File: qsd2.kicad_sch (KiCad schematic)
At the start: 73 parts, among them J1 5-1814832-1, J2 5-1814832-1, J3 Conn_02x08_Odd_Even, J4 SJ-3524-SMT, U1 SN74LVC1G14DBV, U10 GALI-39, U2 SN74LVC1G14DBV, U3 SN74CBT3253, U4 SN74AC74PW, U5 AD8226ARZ-R7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

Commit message: Minor updates to schematic.
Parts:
- C20, C21: value 1nF -> Not used
- R3: value 250 -> 220
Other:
- note added: "5V or 3.3V Option for quadrature and demodulator devices. Place R29 or R30 as required for the chosen device voltage tolerance."
- note removed: "5V or 3.3V Option for demodulator"
- moved on the sheet: R29, R30
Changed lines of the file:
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@@
   (junction (at 91.44 34.29) (diameter 0) (color 0 0 0 0)
   )
-  (junction (at 113.665 146.05) (diameter 0) (color 0 0 0 0)
+  (junction (at 103.505 141.605) (diameter 0) (color 0 0 0 0)
   )
   (junction (at 38.735 170.815) (diameter 0) (color 0 0 0 0)
@@
     (stroke (width 0) (type default))
   )
-  (wire (pts (xy 108.585 141.605) (xy 113.665 141.605))
+  (wire (pts (xy 98.425 137.16) (xy 103.505 137.16))
     (stroke (width 0) (type default))
   )
@@
     (stroke (width 0) (type default))
   )
-  (wire (pts (xy 103.505 151.13) (xy 94.615 151.13))
+  (wire (pts (xy 93.345 146.685) (xy 84.455 146.685))
     (stroke (width 0) (type default))
   )
@@
     (stroke (width 0) (type default))
   )
-  (wire (pts (xy 113.665 146.05) (xy 121.285 146.05))
+  (wire (pts (xy 103.505 141.605) (xy 111.125 141.605))
     (stroke (width 0) (type default))
   )
@@
     (stroke (width 0) (type default))
   )
-  (wire (pts (xy 113.665 146.05) (xy 113.665 151.13))
+  (wire (pts (xy 103.505 141.605) (xy 103.505 146.685))
     (stroke (width 0) (type default))
   )
@@
     (stroke (width 0) (type default))
   )
-  (wire (pts (xy 94.615 141.605) (xy 103.505 141.605))
+  (wire (pts (xy 84.455 137.16) (xy 93.345 137.16))
     (stroke (width 0) (type default))
   )
@@
     (stroke (width 0) (type default))
   )
-  (wire (pts (xy 113.665 141.605) (xy 113.665 146.05))
+  (wire (pts (xy 103.505 137.16) (xy 103.505 141.605))
     (stroke (width 0) (type default))
   )
@@
     (stroke (width 0) (type default))
   )
-  (wire (pts (xy 108.585 151.13) (xy 113.665 151.13))
+  (wire (pts (xy 98.425 146.685) (xy 103.505 146.685))
     (stroke (width 0) (type default))
   )
@@
     (effects (font (size 2 2) bold) (justify left bottom))
   )
-  (text "5V or 3.3V Option\nfor demodulator" (at 116.84 153.035 0)
+  (text "5V or 3.3V Option\nfor quadrature and demodulator\ndevices.  Place R29 or R30 as\nrequired for the chosen device\nvoltage tolerance."
+    (at 105.41 153.67 0)
     (effects (font (size 1.27 1.27)) (justify left bottom))
   )
@@
     (effects (font (size 1.27 1.27)) (justify left bottom))
   )
-  (label "3_3V_FILT" (at 94.615 151.13 0) (fields_autoplaced)
+  (label "3_3V_FILT" (at 84.455 146.685 0) (fields_autoplaced)
     (effects (font (size 1.27 1.27)) (justify left bottom))
   )
-  (label "QSD_V" (at 121.285 146.05 0) (fields_autoplaced)
+  (label "QSD_V" (at 111.125 141.605 0) (fields_autoplaced)
     (effects (font (size 1.27 1.27)) (justify left bottom))
   )
-  (label "5V_FILT" (at 94.615 141.605 0) (fields_autoplaced)
+  (label "5V_FILT" (at 84.455 137.16 0) (fields_autoplaced)
     (effects (font (size 1.27 1.27)) (justify left bottom))
   )
@@
     )
   )
-  (symbol (lib_id "Device:R_Small_US") (at 106.045 151.13 90) (unit 1)
+  (symbol (lib_id "Device:R_Small_US") (at 95.885 146.685 90) (unit 1)
     (in_bom yes) (on_board yes) (dnp no) (fields_autoplaced)
-    (property "Reference" "R30" (at 106.045 145.415 90)
+    (property "Reference" "R30" (at 95.885 140.97 90)
       (effects (font (size 1.27 1.27)))
     )
-    (property "Value" "0" (at 106.045 147.955 90)
+    (property "Value" "0" (at 95.885 143.51 90)
       (effects (font (size 1.27 1.27)))
     )
-    (property "Footprint" "Resistor_SMD:R_1206_3216Metric" (at 106.045 151.13 0)
+    (property "Footprint" "Resistor_SMD:R_1206_3216Metric" (at 95.885 146.685 0)
       (effects (font (size 1.27 1.27)) hide)
     )
-    (property "Datasheet" "~" (at 106.045 151.13 0)
+    (property "Datasheet" "~" (at 95.885 146.685 0)
       (effects (font (size 1.27 1.27)) hide)
     )
@@
   (symbol (lib_id "Device:R_Small_US") (at 55.245 93.98 0) (unit 1)
     (in_bom yes) (on_board yes) (dnp no) (fields_autoplaced)
-    (property "Reference" "R3" (at 57.785 92.71 0)
+    (property "Reference" "R3" (at 57.15 92.71 0)
       (effects (font (size 1.27 1.27)) (justify left))
     )
-    (property "Value" "250" (at 57.785 95.25 0)
+    (property "Value" "220" (at 57.15 95.25 0)
       (effects (font (size 1.27 1.27)) (justify left))
     )
@@
     )
   )
-  (symbol (lib_id "Device:R_Small_US") (at 106.045 141.605 90) (unit 1)
+  (symbol (lib_id "Device:R_Small_US") (at 95.885 137.16 90) (unit 1)
     (in_bom yes) (on_board yes) (dnp no) (fields_autoplaced)
-    (property "Reference" "R29" (at 106.045 135.89 90)
+    (property "Reference" "R29" (at 95.885 131.445 90)
       (effects (font (size 1.27 1.27)))
     )
-    (property "Value" "0" (at 106.045 138.43 90)
+    (property "Value" "0" (at 95.885 133.985 90)
       (effects (font (size 1.27 1.27)))
     )
-    (property "Footprint" "Resistor_SMD:R_1206_3216Metric" (at 106.045 141.605 0)
+    (property "Footprint" "Resistor_SMD:R_1206_3216Metric" (at 95.885 137.16 0)
       (effects (font (size 1.27 1.27)) hide)
     )
-    (property "Datasheet" "~" (at 106.045 141.605 0)
+    (property "Datasheet" "~" (at 95.885 137.16 0)
       (effects (font (size 1.27 1.27)) hide)
     )
@@
   (symbol (lib_id "Device:C_Small") (at 247.65 114.3 90) (unit 1)
     (in_bom yes) (on_board yes) (dnp no) (fields_autoplaced)
-    (property "Reference" "C20" (at 247.6563 107.315 90)
+    (property "Reference" "C20" (at 247.6563 107.95 90)
       (effects (font (size 1.27 1.27)))
     )
-    (property "Value" "1nF" (at 247.6563 109.855 90)
+    (property "Value" "Not used" (at 247.6563 110.49 90)
       (effects (font (size 1.27 1.27)))
     )
@@
       (effects (font (size 1.27 1.27)))
     )
-    (property "Value" "1nF" (at 247.6563 99.06 90)
+    (property "Value" "Not used" (at 247.6563 99.06 90)
       (effects (font (size 1.27 1.27)))
     )

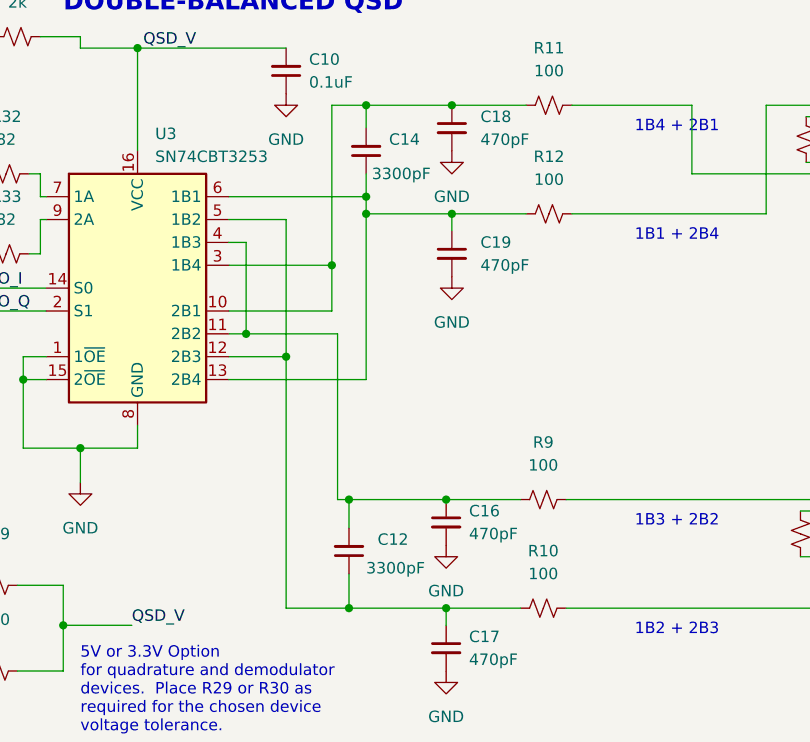
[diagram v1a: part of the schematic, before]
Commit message: Very minor change to silkscreen.  Two capacitors 3300pF to 2200pF.
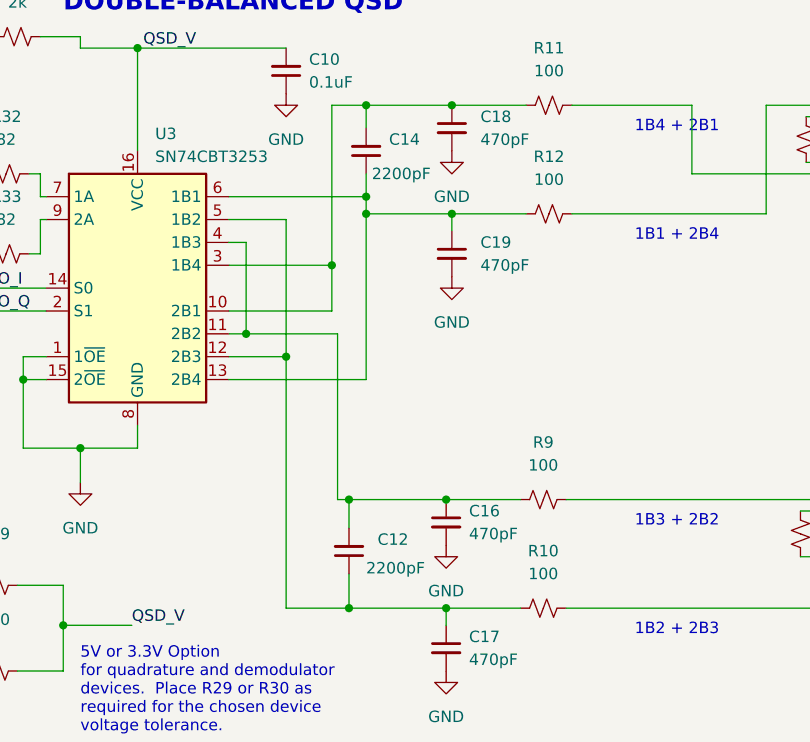
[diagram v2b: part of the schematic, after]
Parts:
- C12, C14: value 3300pF -> 2200pF
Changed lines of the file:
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@@
       (effects (font (size 1.27 1.27)) (justify right))
     )
-    (property "Value" "3300pF" (at 137.16 135.255 0)
+    (property "Value" "2200pF" (at 137.16 135.255 0)
       (effects (font (size 1.27 1.27)) (justify right))
     )
@@
       (effects (font (size 1.27 1.27)) (justify right))
     )
-    (property "Value" "3300pF" (at 137.795 91.44 0)
-      (effects (font (size 1.27 1.27)) (justify right))
-    )
+    (property "Value" "2200pF" (at 137.795 91.44 0)
+      (effects (font (size 1.27 1.27)) (justify right))
+    )

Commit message: Added README.md.
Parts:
- U3: footprint Package_SO:SSOP-16_4.4x5.2mm_P0.65mm -> 16TSOP:DBQ16-L
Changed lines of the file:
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@@
       (effects (font (size 1.27 1.27)) (justify left))
     )
-    (property "Footprint" "Package_SO:SSOP-16_4.4x5.2mm_P0.65mm" (at 111.76 104.14 0)
+    (property "Footprint" "16TSOP:DBQ16-L" (at 111.76 104.14 0)
       (effects (font (size 1.27 1.27)) hide)
     )

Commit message: Updated to version 1.1 PCB.  Very minor changes.
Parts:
- added R16: 0, Resistor_SMD:R_1206_3216Metric, symbol Device:R_Small_US
- R3: value 220 -> 270
- U3: footprint 16TSOP:DBQ16-L -> Package_SO:TSSOP-16_4.4x5mm_P0.65mm
- U4: footprint SN74AC74PW:SOP65P640X120-14N -> Package_SO:TSSOP-14_4.4x5mm_P0.65mm
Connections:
- net REF_I: now also R16.2
- net REF_Q: now also R16.1
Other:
- note added: "Option for using a single reference source"
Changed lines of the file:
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@@
+    (stroke (width 0) (type default))
+  )
+  (wire (pts (xy 246.38 68.58) (xy 255.27 68.58))
     (stroke (width 0) (type default))
   )
@@
     (stroke (width 0) (type default))
   )
+  (wire (pts (xy 260.35 68.58) (xy 267.97 68.58))
+    (stroke (width 0) (type default))
+  )
   (wire (pts (xy 193.04 133.985) (xy 193.04 132.715))
     (stroke (width 0) (type default))
@@
   (wire (pts (xy 100.965 76.2) (xy 105.41 76.2))
     (stroke (width 0) (type default))
+  )
+  (text "Option for using a\nsingle reference source" (at 248.285 74.93 0)
+    (effects (font (size 1.27 1.27)) (justify left bottom))
   )
   (text "1B2 + 2B3" (at 167.005 142.875 0)
@@
     (effects (font (size 1.27 1.27)) (justify left bottom))
   )
+  (label "REF_I" (at 246.38 68.58 0) (fields_autoplaced)
+    (effects (font (size 1.27 1.27)) (justify left bottom))
+  )
   (label "QSD_V" (at 111.125 141.605 0) (fields_autoplaced)
     (effects (font (size 1.27 1.27)) (justify left bottom))
@@
   )
   (label "FB1" (at 175.26 46.355 0) (fields_autoplaced)
+    (effects (font (size 1.27 1.27)) (justify left bottom))
+  )
+  (label "REF_Q" (at 267.97 68.58 0) (fields_autoplaced)
     (effects (font (size 1.27 1.27)) (justify left bottom))
   )
@@
     )
   )
+  (symbol (lib_id "Device:R_Small_US") (at 257.81 68.58 270) (unit 1)
+    (in_bom yes) (on_board yes) (dnp no) (fields_autoplaced)
+    (property "Reference" "R16" (at 257.81 62.23 90)
+      (effects (font (size 1.27 1.27)))
+    )
+    (property "Value" "0" (at 257.81 64.77 90)
+      (effects (font (size 1.27 1.27)))
+    )
+    (property "Footprint" "Resistor_SMD:R_1206_3216Metric" (at 257.81 68.58 0)
+      (effects (font (size 1.27 1.27)) hide)
+    )
+    (property "Datasheet" "~" (at 257.81 68.58 0)
+      (effects (font (size 1.27 1.27)) hide)
+    )
+    (pin "1")
+    (pin "2")
+    (instances
+      (project "qsd2"
+        (path "/e85a7744-7948-44f7-b41f-dd9b75249984"
+          (reference "R16") (unit 1)
+        )
+      )
+    )
+  )
   (symbol (lib_id "Device:FerriteBead_Small") (at 68.58 168.275 90) (unit 1)
     (in_bom yes) (on_board yes) (dnp no)
@@
       (effects (font (size 1.27 1.27)))
     )
-    (property "Footprint" "SN74AC74PW:SOP65P640X120-14N" (at 125.095 46.99 0)
+    (property "Footprint" "Package_SO:TSSOP-14_4.4x5mm_P0.65mm" (at 125.095 46.99 0)
       (effects (font (size 1.27 1.27)) (justify bottom) hide)
     )
@@
       (effects (font (size 1.27 1.27)) (justify left))
     )
-    (property "Value" "220" (at 57.15 95.25 0)
+    (property "Value" "270" (at 57.15 95.25 0)
       (effects (font (size 1.27 1.27)) (justify left))
     )
@@
       (effects (font (size 1.27 1.27)) (justify left))
     )
-    (property "Footprint" "16TSOP:DBQ16-L" (at 111.76 104.14 0)
-      (effects (font (size 1.27 1.27)) hide)
-    )
+    (property "Footprint" "Package_SO:TSSOP-16_4.4x5mm_P0.65mm" (at 111.76 104.14 0)
+      (effects (font (size 1.27 1.27)) hide)
+    )

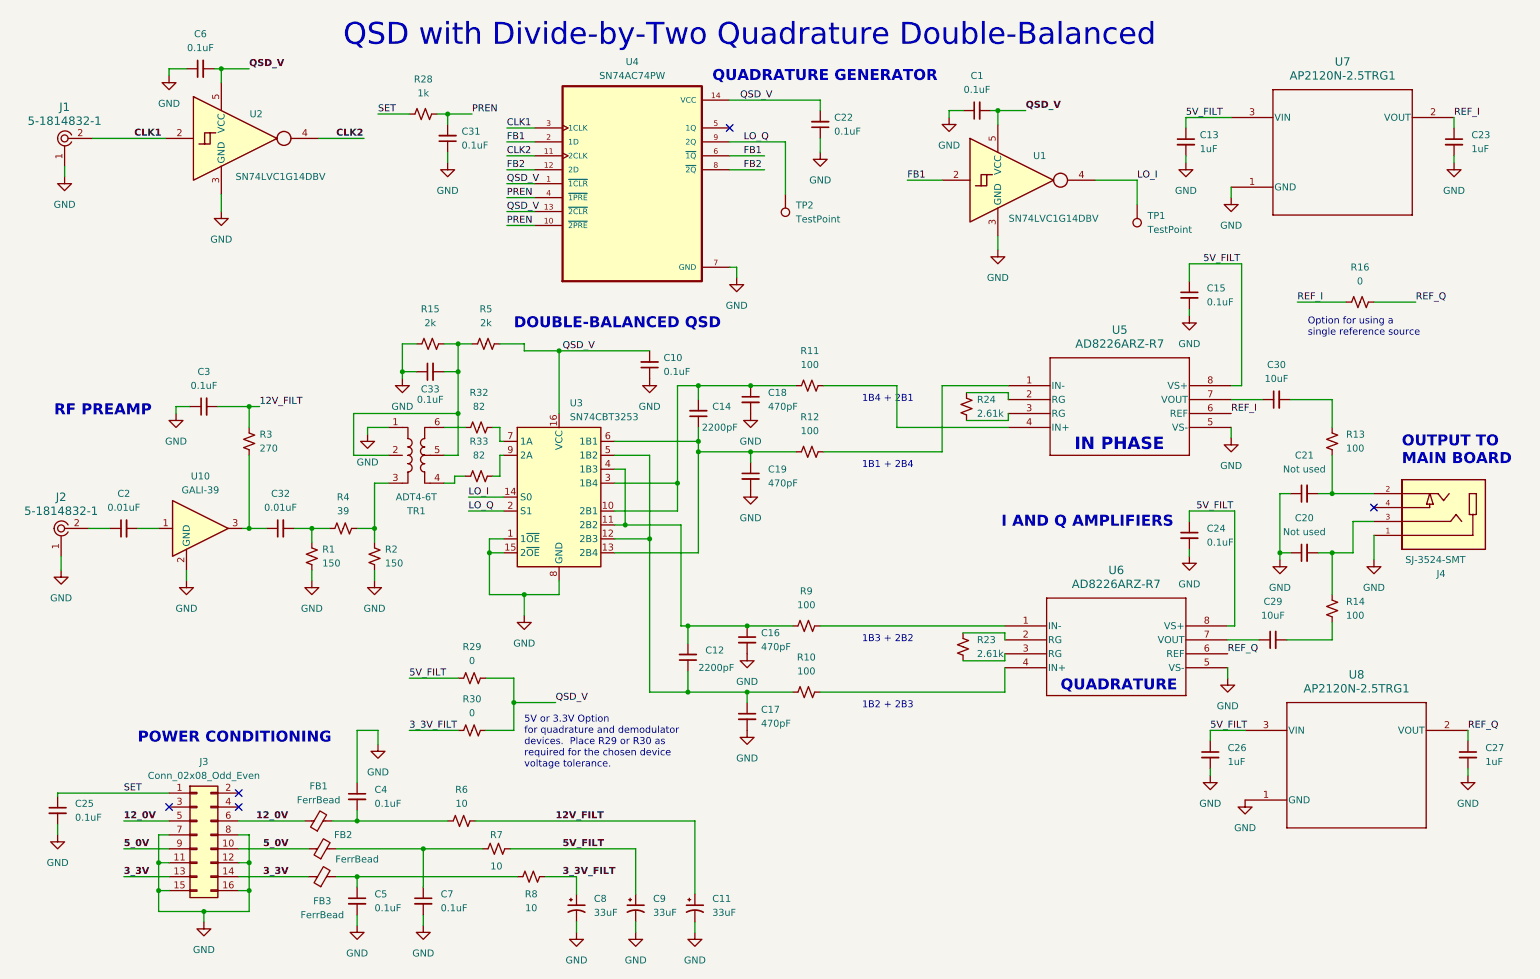
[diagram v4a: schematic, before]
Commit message: Mostly done rotating flip-flop and detector.
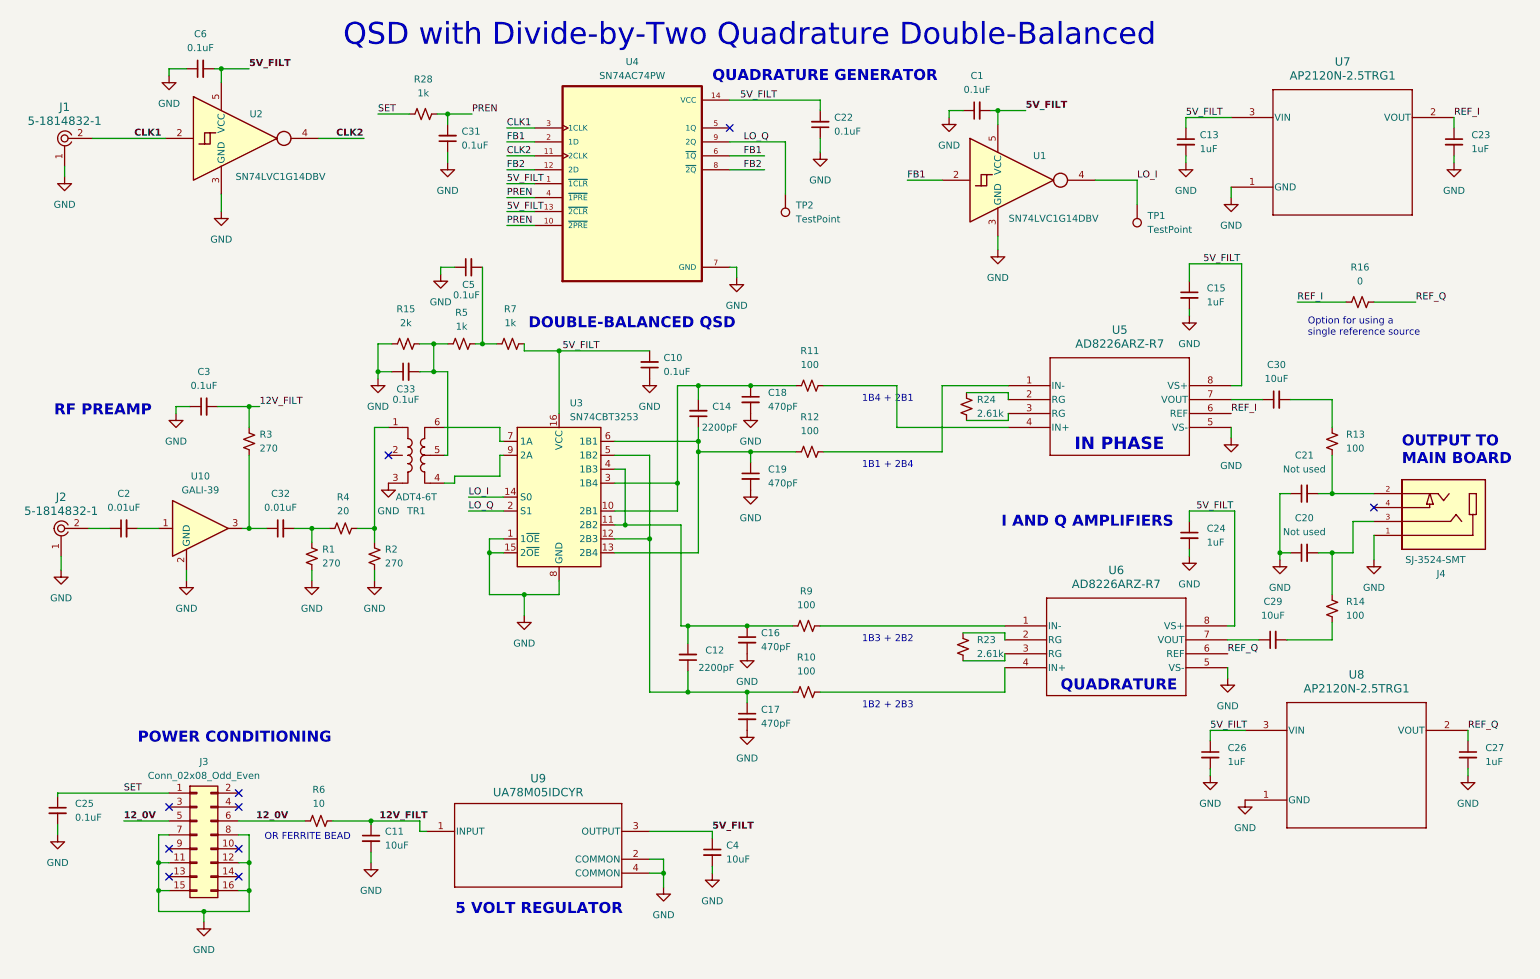
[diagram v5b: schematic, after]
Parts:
- removed C7: 0.1uF, Capacitor_SMD:C_1206_3216Metric, symbol Device:C_Small
- removed C8, C9: 33uF, Capacitor_THT:CP_Radial_D5.0mm_P2.00mm, symbol Device:C_Polarized_Small_US
- removed FB1, FB2, FB3: FerrBead, Inductor_SMD:L_1206_3216Metric, symbol Device:FerriteBead_Small
- removed R29, R30: 0, Resistor_SMD:R_1206_3216Metric, symbol Device:R_Small_US
- removed R32, R33: 82, Resistor_SMD:R_1206_3216Metric, symbol Device:R_Small_US
- removed R8: 10, Resistor_SMD:R_1206_3216Metric, symbol Device:R_Small_US
- added U9: UA78M05IDCYR, DCY0004A_N, symbol UA78M05IDCYR:UA78M05IDCYR
- C11: value 33uF -> 10uF; footprint Capacitor_THT:CP_Radial_D5.0mm_P2.00mm -> Capacitor_SMD:C_1206_3216Metric; symbol Device:C_Polarized_Small_US -> Device:C_Small
- C15, C24: value 0.1uF -> 1uF
- C4: value 0.1uF -> 10uF
- R1, R2: value 150 -> 270
- R4: value 39 -> 20
- R5: value 2k -> 1k
- R7: value 10 -> 1k
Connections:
- net 12V_FILT: now also U9.1 (INPUT)
- net 12_0V: now also R6.1
- net 5V_FILT: now also C1.2, C10.2, C22.2, C4.1, C6.2, U1.5 (VCC), U2.5 (VCC), U3.16 (VCC), U4.1 (~{1CLR}), U4.13 (~{2CLR}), U4.14 (VCC), U9.3 (OUTPUT)
- net GND: now also C4.2, C5.1, TR1.3, U9.2 (COMMON), U9.4 (COMMON); no longer C4.1, C5.2, TR1.1
- net at C33.2, R15.2, R5.1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: no longer TR1.2 (NOCONN)
- net at R2.1, R4.2: now also TR1.1; no longer TR1.3
- net at R7.1: now also C5.2, R5.2
- net at TR1.4: now also U3.9 (2A)
- net at TR1.6: now also U3.7 (1A)
- net 3_3V: no longer names the net of J3.13 (Pin_13)
- net 3_3V: no longer J3.14 (Pin_14)
- net 5_0V: no longer names the net of J3.10 (Pin_10)
- net 5_0V: no longer J3.9 (Pin_9)
- removed net QSD_V: C1.2, C10.2, C22.2, C6.2, R5.2, U1.5 (VCC), U2.5 (VCC), U3.16 (VCC), U4.1 (~{1CLR}), U4.13 (~{2CLR}), U4.14 (VCC)
- no-connect marks 5 -> 10
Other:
- note added: "5 VOLT REGULATOR"
- note added: "OR FERRITE BEAD"
- note removed: "5V or 3.3V Option for quadrature and demodulator devices. Place R29 or R30 as required for the chosen device voltage tolerance."
- moved on the sheet: C33, R15, R5, R6
